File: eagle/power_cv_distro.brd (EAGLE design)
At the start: 101.6 x 80 mm, 51 parts, among them U1 POWER, U10 TLV2372IP, U11 TLV2372IP, U12 TLV2372IP, U13 TLV2372IP, U2 POWER, U3 POWER, U4 POWER, U5 POWER, U6 POWER, U7 POWER, U8 POWER, U9 POWER

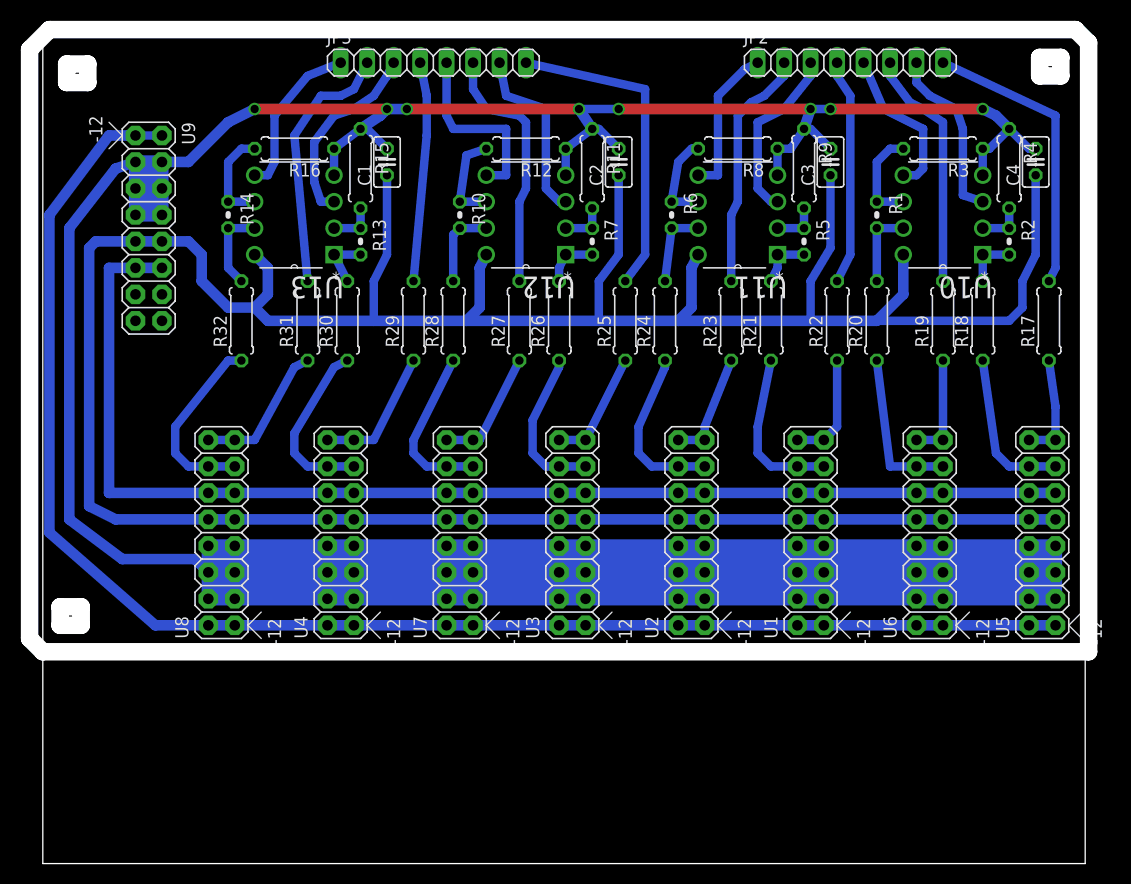
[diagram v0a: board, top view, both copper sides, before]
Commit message: filtering power for scale opamps
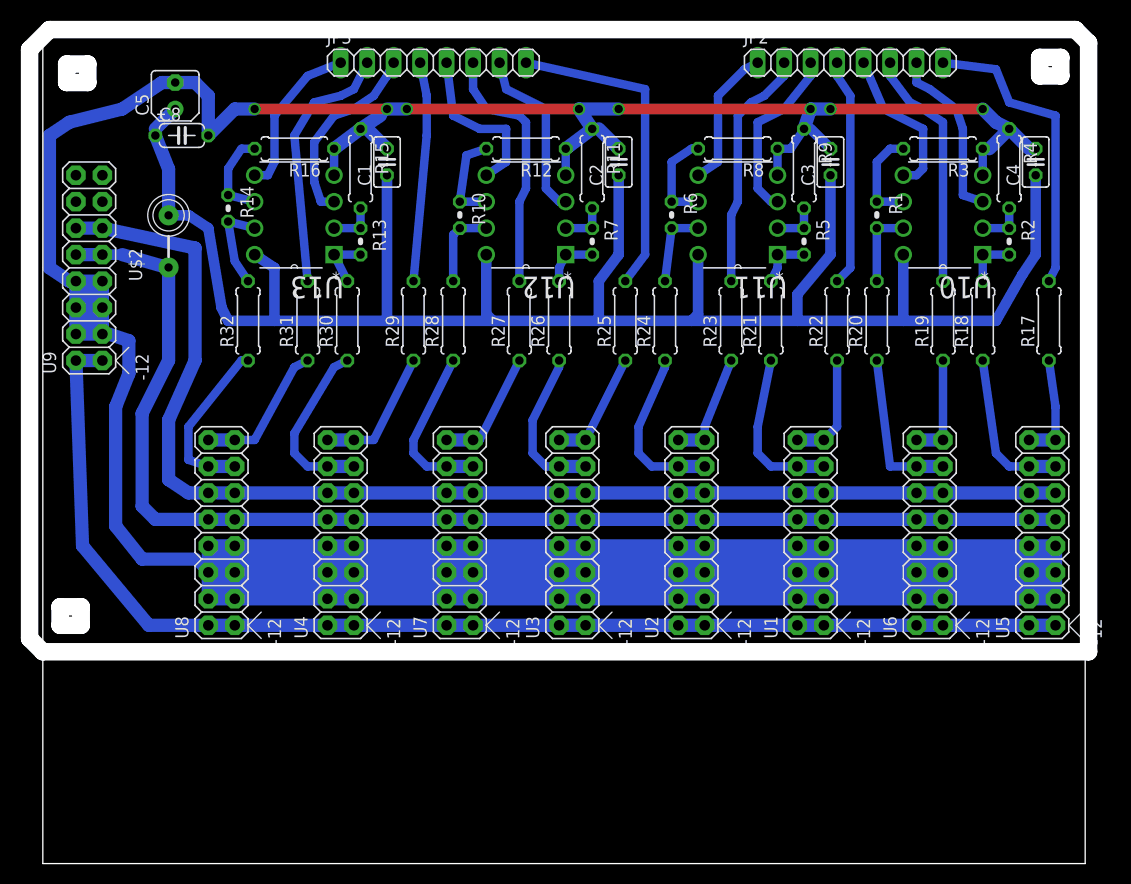
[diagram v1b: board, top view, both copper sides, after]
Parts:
- added C5: 10u, rcl:B45181A
- added C8: 100n, rcl:C050-024X044
- added U$2: FB, adafruit:FB
- moved U9 10.6 mm to (4.45, 54.6), turned to 90 degrees
- moved R14 0.64 mm to (17.8, 62.9)
- moved R32 0.63 mm to (19.7, 52.1)
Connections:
- new net N$49: U1.10, U1.9, U2.10, U2.9, U3.10, U3.9, U4.10, U4.9, U5.10, U5.9, U6.10, U6.9, U7.10, U7.9, U8.10, U8.9
- new net VDD: C1.1, C2.1, C3.1, C4.1, C5.+, C8.1, U$2.P$2, U10.8, U11.8, U12.8, U13.8
- net +12V: now also U$2.P$1; no longer C1.1, C2.1, C3.1, C4.1, U1.10, U1.9, U10.8, U11.8, U12.8, U13.8, U2.10, U2.9, U3.10, U3.9, U4.10, U4.9, U5.10, U5.9, U6.10, U6.9, U7.10, U7.9, U8.10, U8.9
- net GND: now also C5.-, C8.2
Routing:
- net +12V: track 296.7 -> 9.69 mm
- net VDD: track 0.00 -> 183.9 mm
- net N$49: track 0.00 -> 116.2 mm
- net -12V: track 144.9 -> 117.2 mm
- net GND: track 185.4 -> 201.0 mm
- net +5V: track 117.5 -> 119.9 mm
- net N$12: track 17.9 -> 16.0 mm
- net N$48: track 18.2 -> 16.5 mm
- net N$1: track 28.0 -> 29.2 mm
- net N$8: track 14.5 -> 13.7 mm
- net N$32: track 9.42 -> 8.72 mm
- net N$29: track 8.15 -> 8.77 mm
